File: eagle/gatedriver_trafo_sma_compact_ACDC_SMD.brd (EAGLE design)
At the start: 128.5 x 101.9 mm, 14 parts

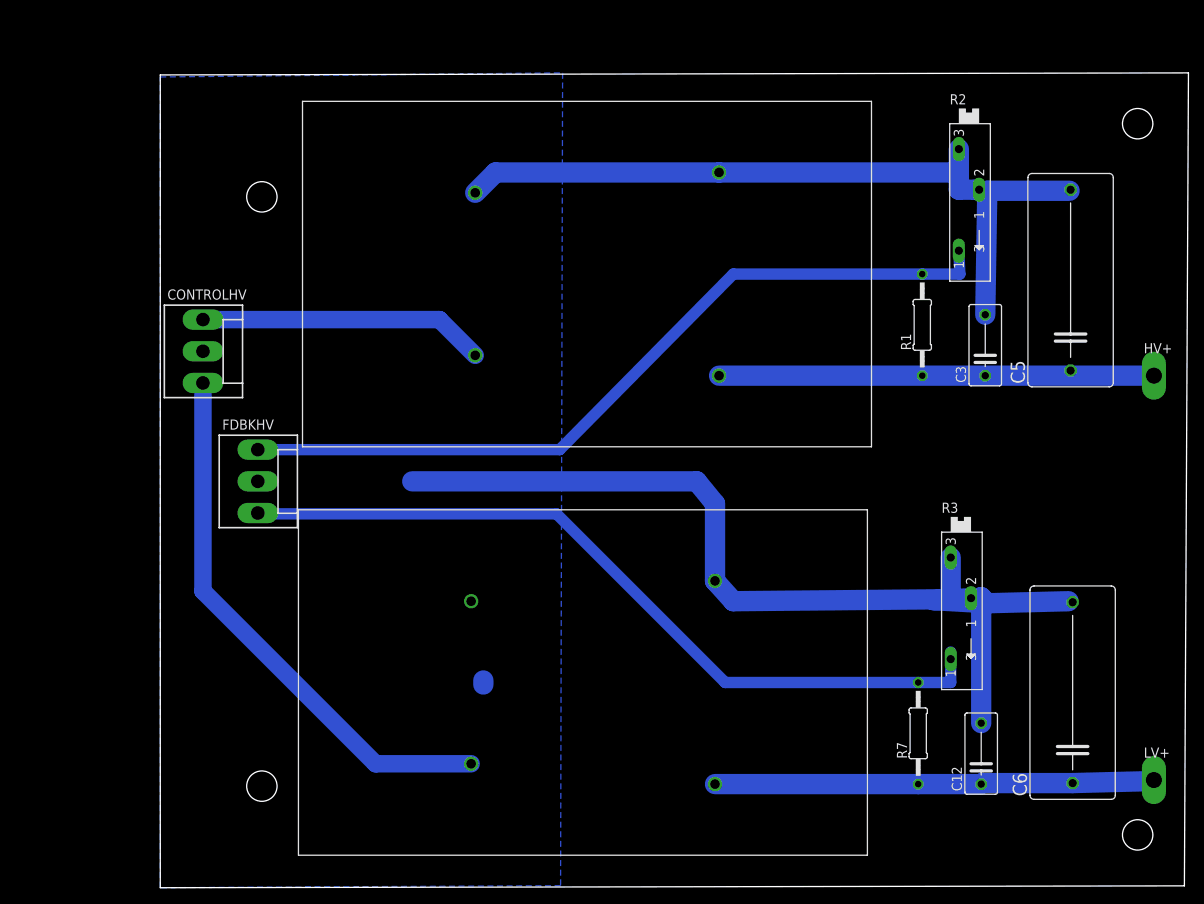
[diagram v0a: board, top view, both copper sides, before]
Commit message: 3PS, 2 1kV in parallel
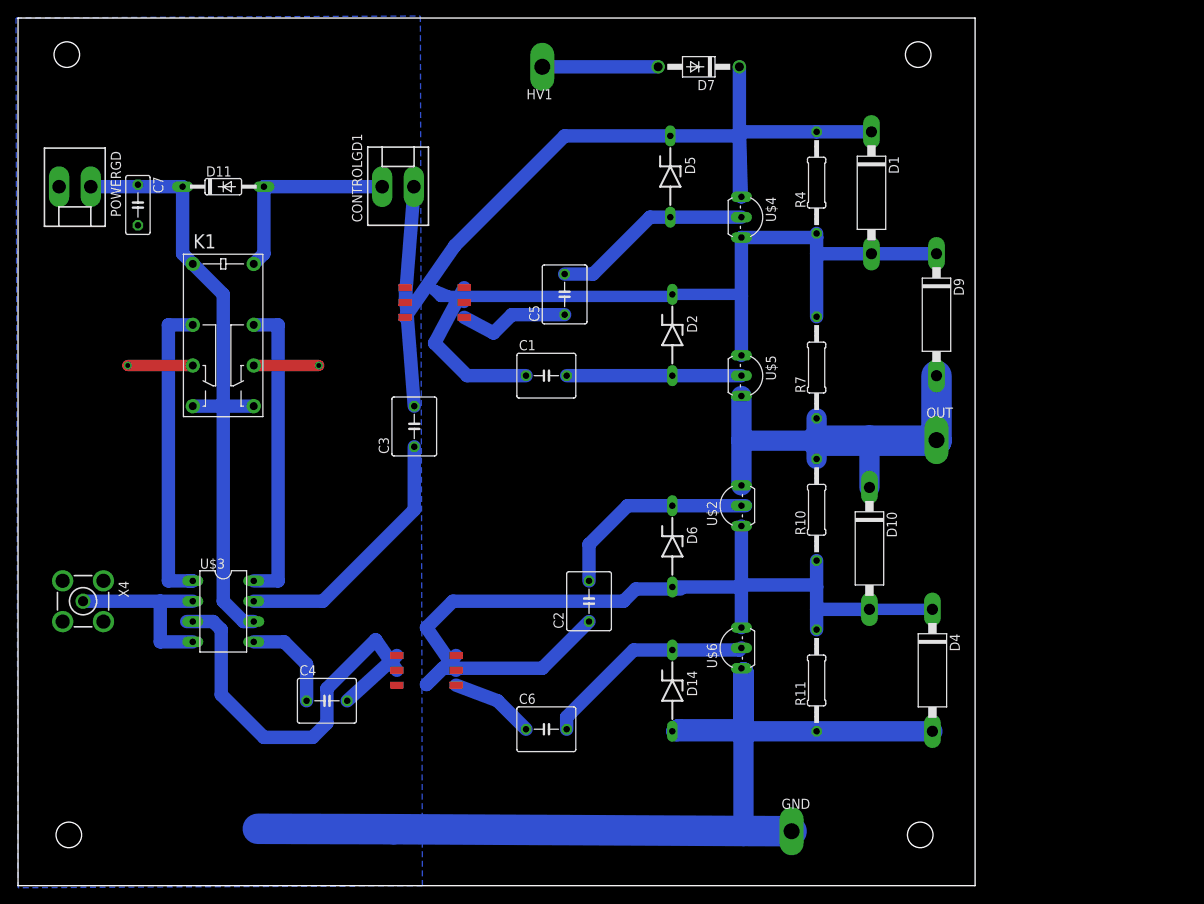
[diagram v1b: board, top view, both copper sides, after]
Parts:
- removed C12: .01u, rcl:C075-042X103
- removed CONTROLHV, FDBKHV: (no value), con-molex:KK-156-3
- removed HV+, LV+: TPPAD1-20Y, testpad:P1-20Y
- removed R1: 2M, resistor:0207/12
- removed R2, R3: (no value), pot:SP19L
- added C1, C2, C4: (no value), resistor:C050-055X075
- added C7: (no value), rcl:C050-030X075
- added CONTROLGD1, POWERGD: (no value), con-molex:KK-156-2
- added D1, D10, D4, D9: P6KEXXA, diode:C1702-15
- added D11: 1N4148DO35-10, diode:DO35-10
- added D14, D2, D5, D6: 4742, diode:ZDIO-10
- added D7: 1N4004, diode:DO41-10
- added GND, HV1, OUT: TPPAD1-20Y, testpad:P1-20Y
- added K1: G5V-2, relay:G5V-2
- added R10, R11, R4: 1M, rcl:0207/12
- added U$3: UCC27425, texas:DIL08
- added U$4, U$5: VP0550, transistor-fet:TO92-
- added U$6: VN0550, transistor-fet:TO92-
- added U$7: DA-2320SMD6, trafo:SMD6
- added X4: BU-SMA-V, con-coax:BU-SMA-V
- C3: value .01u -> (none); device rcl:C075-042X103 -> resistor:C050-055X075
- C5, C6: value 1u -> (none); device rcl:C225-108X268 -> resistor:C050-055X075
- R7: value 2M -> 1M; device resistor:0207/12 -> rcl:0207/12
- U$1: value EMCO-F104PIN -> DA-2320SMD6; device dc-dc-converter:EMCO-F -> trafo:SMD6
- U$2: value EMCO-F104PIN -> VN0550; device dc-dc-converter:EMCO-F -> transistor-fet:TO92-
- moved C3 72.1 mm to (49.5, 57.4)
- moved C6 65.9 mm to (66.0, 19.6), turned to 0 degrees
- moved C5 63.3 mm to (68.3, 73.9)
- moved R7 47.5 mm to (99.8, 64.8)
- moved U$2 46.7 mm to (90.4, 47.5), turned to 90 degrees
- moved U$1 8.33 mm to (52.1, 72.9)
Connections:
- removed net N$8: FDBKHV.3, R3.A, R7.2
- new net +15V: C7.1, D11.C, K1.1, K1.8, K1.9, POWERGD.1, U$3.6
- new net ENSW: CONTROLGD1.1, D11.A, K1.16
- new net N$11: C1.2, D2.A, U$5.2
- new net N$13: D10.A, D4.C, D6.A, R10.1, R11.2, U$2.3, U$6.1
- new net N$14: K1.4, U$3.1
- new net N$15: K1.13, U$3.8
- new net N$16: C5.2, D5.A, U$4.2
- new net N$17: D1.C, D5.C, D7.C, R4.2, U$1.P$3, U$4.3
- new net N$18: D1.A, D2.C, D9.C, R4.1, R7.2, U$1.P$5, U$4.1, U$5.3
- new net N$21: D10.C, D9.A, OUT.TP, R10.2, R7.1, U$2.1, U$5.1
- new net N$22: C2.1, U$7.P$6
- new net N$23: C6.1, U$7.P$4
- new net N$25: C2.2, D6.C, U$2.2
- new net N$27: C6.2, D14.C, U$6.2
- new net N$29: D7.A, HV1.TP
- new net N$6: C4.2, U$7.P$1
- new net N$7: C5.1, U$1.P$4
- new net N$9: U$7.P$5
- net GND: now also C7.2, CONTROLGD1.2, D14.A, D4.A, GND.TP, K1.11, K1.6, POWERGD.2, R11.1, U$3.3, U$6.3, U$7.P$2, U$7.P$3, X4.2, X4.3, X4.4, X4.5; no longer C12.2, C3.2, C5.2, C6.2, CONTROLHV.2, FDBKHV.2, R2.E, R2.S, R3.E, R3.S, U$1.P$4, U$2.P$2, U$2.P$4
- net N$1: now also U$3.2, U$3.4, X4.1; no longer C3.1, C5.1, HV+.TP, R1.1, U$1.P$3
- net N$2: now also C3.1, U$3.7; no longer C12.1, C6.1, LV+.TP, R7.1, U$2.P$3
- net N$3: now also C3.2, U$1.P$1; no longer FDBKHV.1, R1.2, R2.A
- net N$4: now also C4.1, U$3.5; no longer CONTROLHV.1, U$1.P$1
- net N$5: now also C1.1, U$1.P$6; no longer CONTROLHV.3, U$2.P$1
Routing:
- net N$8: track 99.5 -> 0.00 mm
- net N$17: track 0.00 -> 93.2 mm
- net N$18: track 0.00 -> 92.4 mm
- net N$3: track 99.8 -> 14.9 mm
- net +15V: track 0.00 -> 77.9 mm
- net N$13: track 0.00 -> 55.6 mm
- net N$21: track 0.00 -> 54.6 mm
- net N$5: track 68.5 -> 21.0 mm
- net N$9: track 0.00 -> 40.2 mm
- net N$14: track 0.00 -> 38.6 mm
- net N$15: track 0.00 -> 38.1 mm
- net N$1: track 54.4 -> 22.9 mm
- net N$22: track 0.00 -> 28.8 mm
- net N$27: track 0.00 -> 26.9 mm
- net N$25: track 0.00 -> 26.1 mm
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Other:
- board size 128.5 x 101.9 mm -> 119.6 x 108.5 mm
